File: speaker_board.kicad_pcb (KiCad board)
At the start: 2 copper layers, 3 parts, among them J2 MP3_Module

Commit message: initial pcb
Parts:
- added A1: Arduino_UNO_R3, Module:Arduino_UNO_R3, F.Cu at (196.6, 57.3)
- moved LS1 21.9 mm to (160.5, 80.3), turned to 180 degrees
- moved J2 10.5 mm to (138.3, 77.5), turned to 90 degrees
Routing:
- net Net-(A1-D2): track 0.00 -> 100.5 mm
- net Net-(A1-D3): track 0.00 -> 96.2 mm
- net +5V: track 0.00 -> 77.7 mm
- net GND: track 0.00 -> 74.2 mm
- net Net-(J2-SPK_2): track 0.00 -> 18.4 mm
- net Net-(J2-SPK_1): track 0.00 -> 18.0 mm
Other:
- board outline added: 106.5 x 59 mm

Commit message: UPDATED schematic
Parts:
- removed J2: MP3_Module, Connector_PinSocket_2.54mm:PinSocket_2x08_P2.54mm_Vertical
- added J1: MP3_Module_Left, Connector_PinSocket_2.54mm:PinSocket_1x08_P2.54mm_Vertical, F.Cu at (185.8, 85.5)
- added J3: MP3_Module_Right, Connector_PinSocket_2.54mm:PinSocket_1x08_P2.54mm_Vertical, F.Cu at (185.8, 73.0)
- moved LS1 51.0 mm to (211.5, 80.3)
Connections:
- A1 pad 17: Net-(A1-D2) -> MP3_RX
- A1 pad 18: Net-(A1-D3) -> MP3_TX
- LS1 pad 1: Net-(J2-SPK_1) -> SPK_1
- LS1 pad 2: Net-(J2-SPK_2) -> SPK_2
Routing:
- net Net-(A1-D2): track 100.5 -> 0.00 mm
- net Net-(A1-D3): track 96.2 -> 0.00 mm
- net MP3_RX: track 0.00 -> 48.6 mm
- net MP3_TX: track 0.00 -> 41.9 mm
- net +5V: track 77.7 -> 36.9 mm
- net GND: track 74.2 -> 39.1 mm
- net Net-(J2-SPK_2): track 18.4 -> 0.00 mm
- net Net-(J2-SPK_1): track 18.0 -> 0.00 mm
- net SPK_2: track 0.00 -> 15.2 mm
- net SPK_1: track 0.00 -> 15.1 mm
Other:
- board size 106.5 x 59 mm -> 79 x 59 mm

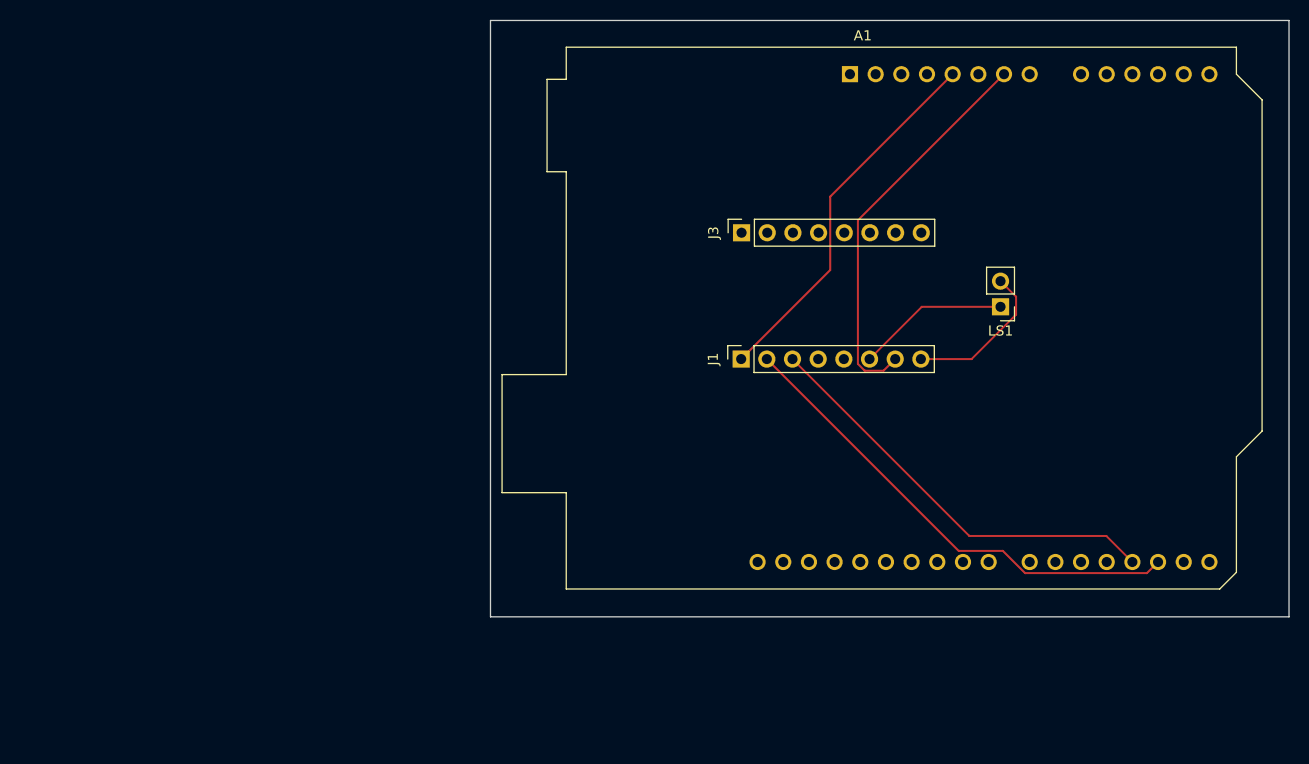
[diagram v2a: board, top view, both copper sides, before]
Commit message: Board with updated components
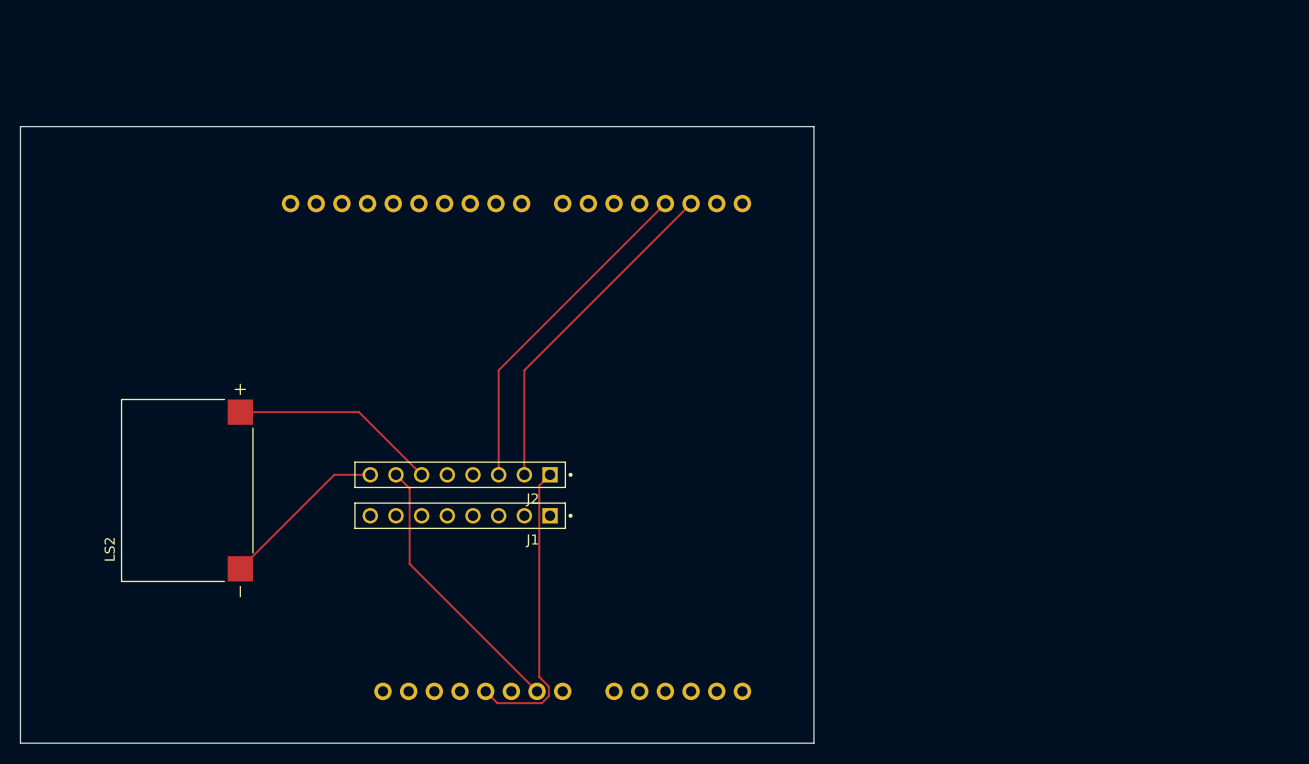
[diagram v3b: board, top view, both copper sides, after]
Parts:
- removed the A1 at (196.6, 57.3)
- removed J3: MP3_Module_Right, Connector_PinSocket_2.54mm:PinSocket_1x08_P2.54mm_Vertical
- removed LS1: Speaker, Connector_PinHeader_2.54mm:PinHeader_1x02_P2.54mm_Vertical
- added A2: ARDUINO_UNO_R3, rsx_modules:STM32_NUCLEO64_ArduinoUno, F.Cu at (122.4, 120.9)
- added J2: MP3_Module, rsx_misc:SAMESKY_SSK02-FPH-254-A8, F.Cu at (158.0, 97.0)
- added LS2: AS01808AO-SC18-WP-R, rsx_sensors:SPKR_AS01808AO-SC18-WP-R, F.Cu at (131.0, 98.5)
- J1: value MP3_Module_Left -> SSK02-FPH-254-A8; footprint Connector_PinSocket_2.54mm:PinSocket_1x08_P2.54mm_Vertical -> rsx_misc:SAMESKY_SSK02-FPH-254-A8
- moved A1 56.2 mm to (169.4, 104.0), turned to 180 degrees
- moved J1 31.8 mm to (158.0, 101.0), turned to 180 degrees
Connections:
- J1 pad 1: +5V -> unconnected-(J1-IO_1-Pad1)
- J1 pad 2: MP3_RX -> unconnected-(J1-GND-Pad2)
- J1 pad 3: MP3_TX -> unconnected-(J1-IO_2-Pad3)
- J1 pad 6: SPK_1 -> unconnected-(J1-USB+-Pad6)
- J1 pad 7: GND -> unconnected-(J1-USB--Pad7)
- J1 pad 8: SPK_2 -> unconnected-(J1-BUSY-Pad8)
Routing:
- net MP3_RX: track 48.6 -> 33.7 mm
- net GND: track 39.1 -> 27.2 mm
- net MP3_TX: track 41.9 -> 33.7 mm
- net +5V: track 36.9 -> 29.7 mm
- net SPK_1: track 15.1 -> 20.5 mm
- net SPK_2: track 15.2 -> 16.7 mm
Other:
- board size 79 x 59 mm -> 78.5 x 61 mm
